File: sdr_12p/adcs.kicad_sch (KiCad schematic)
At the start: 2 parts, among them U10 LT3042xMSE, U3 ADAU1978xBCP

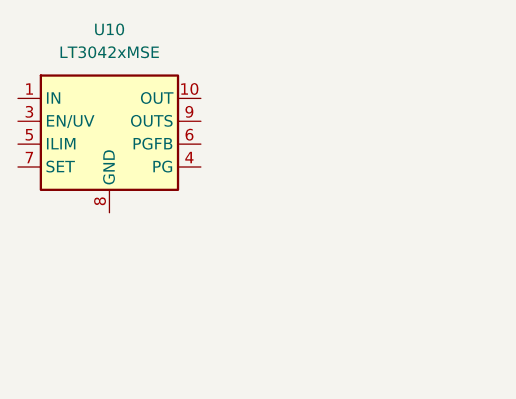
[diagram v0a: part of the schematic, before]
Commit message: added uC
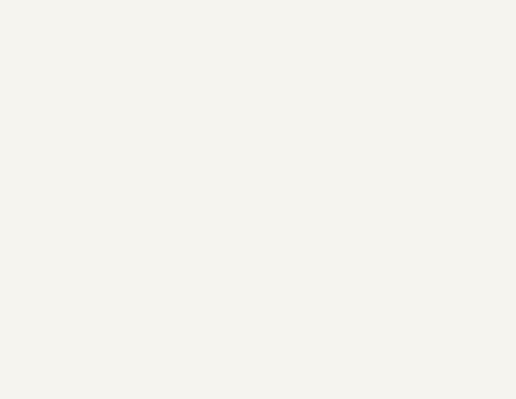
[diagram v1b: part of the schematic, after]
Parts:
- removed U10: LT3042xMSE, Package_SO:MSOP-10-1EP_3x3mm_P0.5mm_EP1.68x1.88mm, symbol Regulator_Linear:LT3042xMSE
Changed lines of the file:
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@@
-		)
-	)
-	(symbol
-		(lib_id "Regulator_Linear:LT3042xMSE")
-		(at 33.02 33.02 0)
-		(unit 1)
-		(exclude_from_sim no)
-		(in_bom yes)
-		(on_board yes)
-		(dnp no)
-		(fields_autoplaced yes)
-		(property "Reference" "U10"
-			(at 33.02 22.86 0)
-			(effects
-				(font
-					(size 1.27 1.27)
-				)
-			)
-		)
-		(property "Value" "LT3042xMSE"
-			(at 33.02 25.4 0)
-			(effects
-				(font
-					(size 1.27 1.27)
-				)
-			)
-		)
-		(property "Footprint" "Package_SO:MSOP-10-1EP_3x3mm_P0.5mm_EP1.68x1.88mm"
-			(at 33.02 24.765 0)
-			(effects
-				(font
-					(size 1.27 1.27)
-				)
-				(hide yes)
-			)
-		)
-		(property "Datasheet" "https://www.analog.com/media/en/technical-documentation/data-sheets/3042fb.pdf"
-			(at 33.02 33.02 0)
-			(effects
-				(font
-					(size 1.27 1.27)
-				)
-				(hide yes)
-			)
-		)
-		(property "Description" "200mA, Adjustable, Ultralow Noise, Ultrahigh PSRR RF Linear Regulator, MSOP-10"
-			(at 33.02 33.02 0)
-			(effects
-				(font
-					(size 1.27 1.27)
-				)
-				(hide yes)
-			)
-		)
-		(pin "11"
-		)
-		(pin "9"
-		)
-		(pin "2"
-		)
-		(pin "1"
-		)
-		(pin "4"
-		)
-		(pin "10"
-		)
-		(pin "8"
-		)
-		(pin "5"
-		)
-		(pin "3"
-		)
-		(pin "6"
-		)
-		(pin "7"
-		)
-		(instances
-			(project "sdr_12p"
-				(path "/fe42ca2f-2bb8-4d5a-9e84-807788ed632f/d1b276aa-cc76-4829-b01b-98095216e3ce"
-					(reference "U10")
-					(unit 1)
-				)
-			)
 		)
 	)
